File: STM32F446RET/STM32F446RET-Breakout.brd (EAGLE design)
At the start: 68.6 x 68.6 mm, 30 parts, among them X1 32.768KHZ

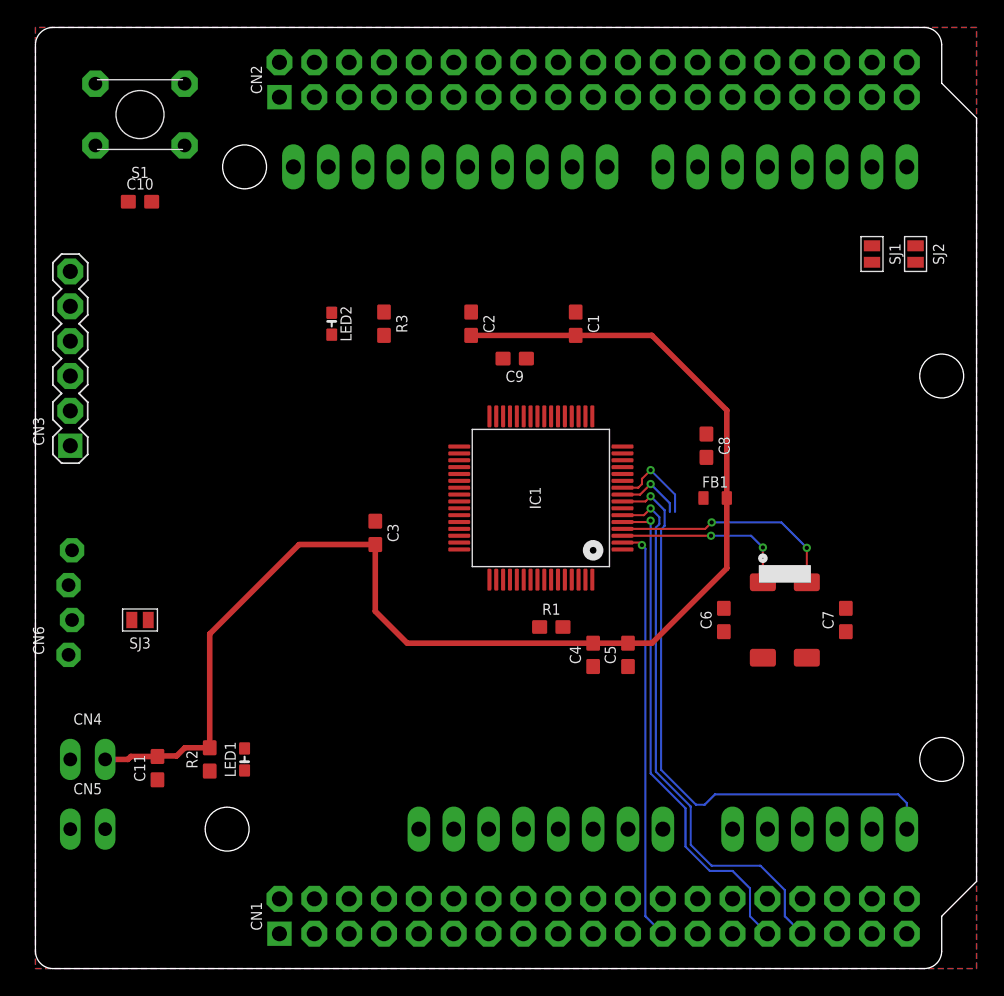
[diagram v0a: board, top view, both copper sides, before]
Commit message: fix STM32F446RET-Breakout Rev.BETA
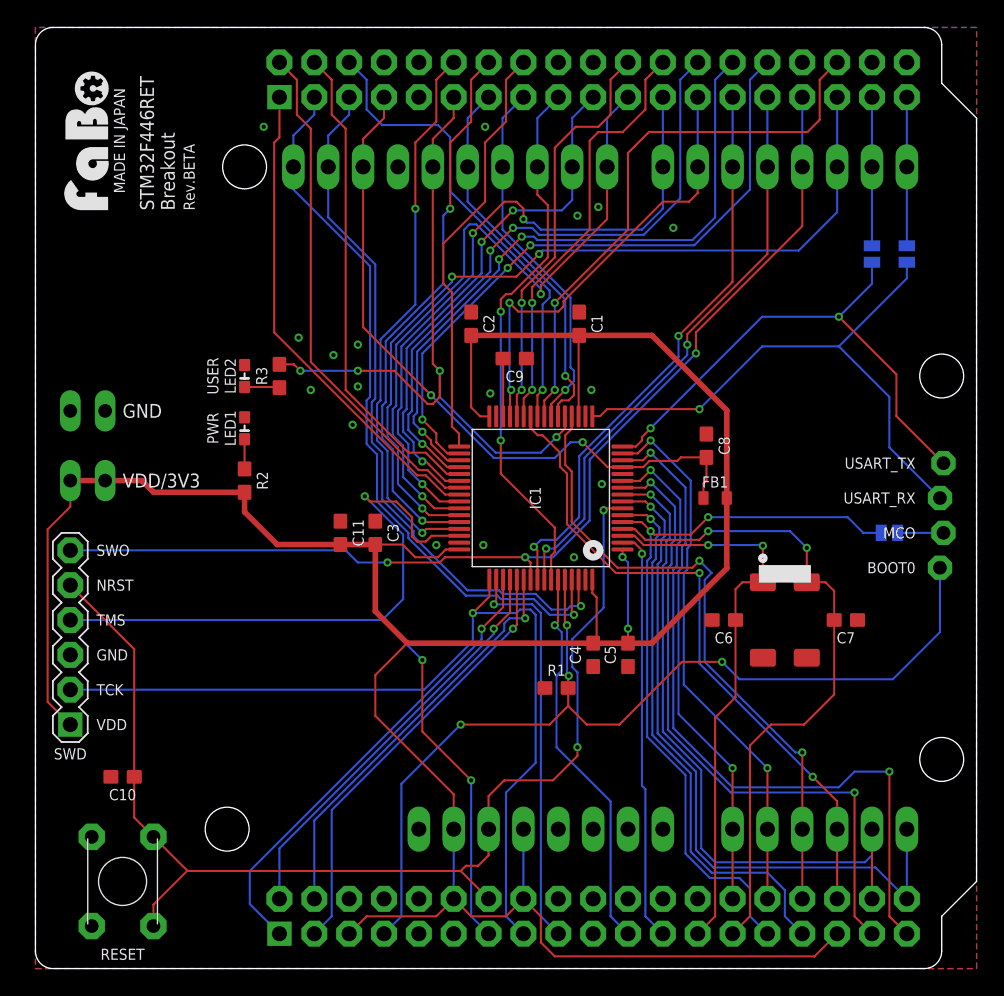
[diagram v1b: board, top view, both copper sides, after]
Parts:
- added U$2: (no value), FaBo-etc:LOGO_FABO_MS
- added U$3: (no value), FaBo-etc:LOGO_OSHW_M_BOTTOM
- moved CN6 63.8 mm to (66.0, 33.0)
- moved S1 55.9 mm to (6.35, 6.35), turned to 270 degrees
- moved SJ3 55.0 mm to (62.2, 31.8), flipped to the bottom
- moved C10 41.9 mm to (6.35, 14.0), turned to 180 degrees
- moved CN5 30.5 mm to (3.81, 40.6)
- moved LED1 24.1 mm to (15.2, 39.4)
- moved C11 21.7 mm to (22.2, 31.8), turned to 270 degrees
- moved R2 20.5 mm to (15.2, 35.6), turned to 270 degrees
- moved CN3 20.3 mm to (2.54, 24.1)
- moved CN4 20.3 mm to (3.81, 35.6)
- moved R3 8.52 mm to (17.8, 43.2), turned to 90 degrees
- moved LED2 7.41 mm to (15.2, 43.2), turned to 90 degrees
- moved R1 4.46 mm to (38.0, 20.4)
- moved SJ2 0.64 mm to (63.5, 52.1), flipped to the bottom
- moved C1 0.25 mm to (39.6, 47.0)
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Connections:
- net N$1 renamed PWRLEDA
- net N$3 renamed USRLEDA
- removed net PB11: C9.2, CN2.18, IC1.30
- new net VCAP_1: C9.2, IC1.30
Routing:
- net 3V3: track 97.1 -> 209.9 mm, vias 0 -> 2
- net NRST: track 0.00 -> 87.2 mm, vias 0 -> 2
- net PB3: track 0.00 -> 78.6 mm, vias 0 -> 3
- net BOOT0: track 0.00 -> 71.5 mm, vias 0 -> 4
- net PA13: track 0.00 -> 68.8 mm, vias 0 -> 3
- net PA14: track 0.00 -> 65.3 mm, vias 0 -> 1
- net PA10: track 0.00 -> 61.2 mm, vias 0 -> 3
- net PB8: track 0.00 -> 53.5 mm, vias 0 -> 1
- net PC3: track 0.00 -> 52.6 mm, vias 0 -> 2
- net PB9: track 0.00 -> 51.9 mm, vias 0 -> 1
- net AVDD: track 0.00 -> 50.9 mm, vias 0 -> 2
- net PA9: track 0.00 -> 50.6 mm, vias 0 -> 2
- net PA5: track 0.00 -> 50.1 mm, vias 0 -> 4
- net PA8: track 0.00 -> 49.3 mm, vias 0 -> 3
- net PB0: track 0.00 -> 48.2 mm, vias 0 -> 2
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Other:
- board text added: "BOOT0"
- board text added: "GND"
- board text added: "MADE IN JAPAN"
- board text added: "MCO"
- board text added: "NRST"
- board text added: "PWR"
- board text added: "RESET"
- board text added: "Rev.BETA"
- board text added: "STM32F446RET Breakout"
- board text added: "SWD"
- board text added: "SWO"
- board text added: "TCK"
- board text added: "TMS"
- board text added: "USART_RX"
- board text added: "USART_TX"
- board text added: "USER"
- board text added: "VDD"
- board text added: "VDD/3V3"
